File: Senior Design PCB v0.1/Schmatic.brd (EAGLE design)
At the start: 101.3 x 67.5 mm, 243 parts, among them IC1 TMC2208, IC2 TMC2208, IC3 TMC2208, IC4 TMC2208, IC5 TMC2208, IC6 CP2104, Q1 mmbt2222, Q2 mmbt2222, Q3 MMBT4403, Q4 AOD417, Q5 MMBT4403, Q6 MMBT4403, Q7 DMG3415U, U1 PCA9685, U2 AP2112-3.3, U3 HTU21DF, U4 HX711, U5 HX711, U6 HX711, U7 SX1509, X2 ESP32_WROOM32_SKINNY

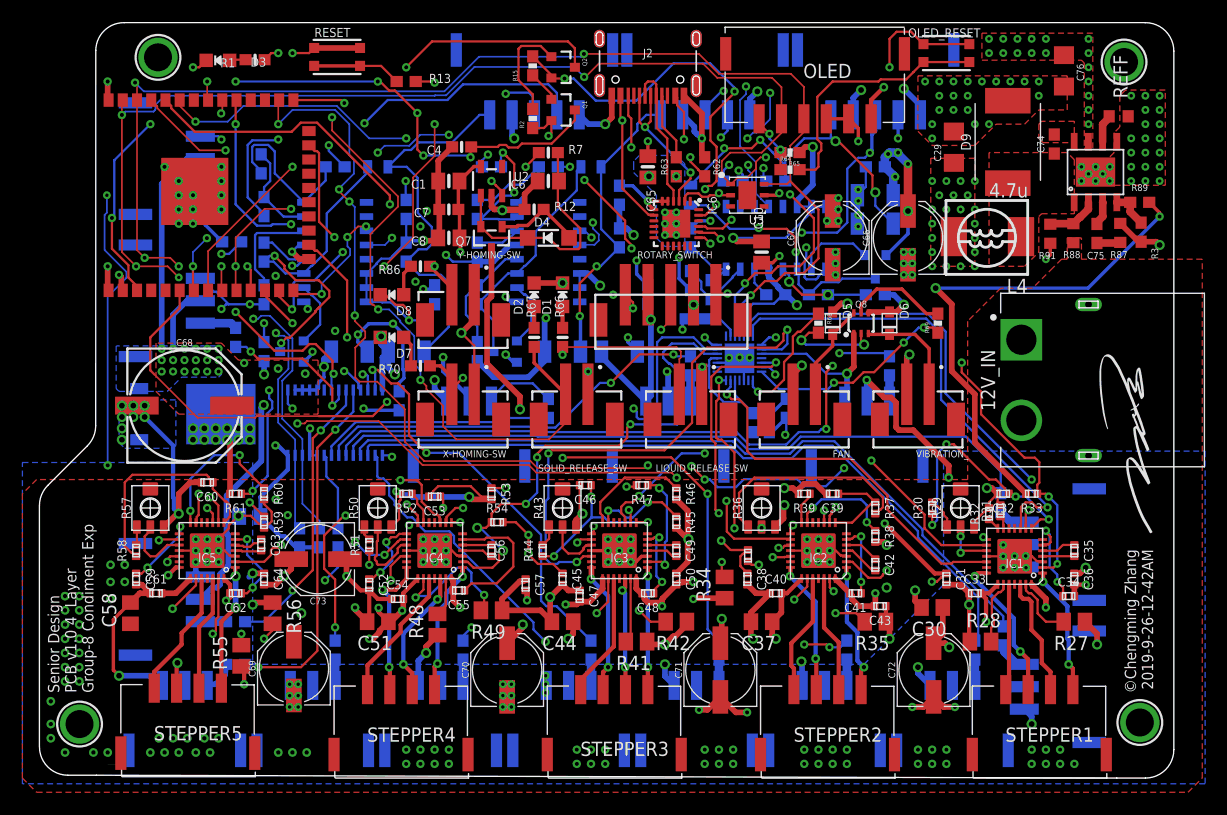
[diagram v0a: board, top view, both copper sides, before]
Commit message: added another buck converter for 5v to 3v3
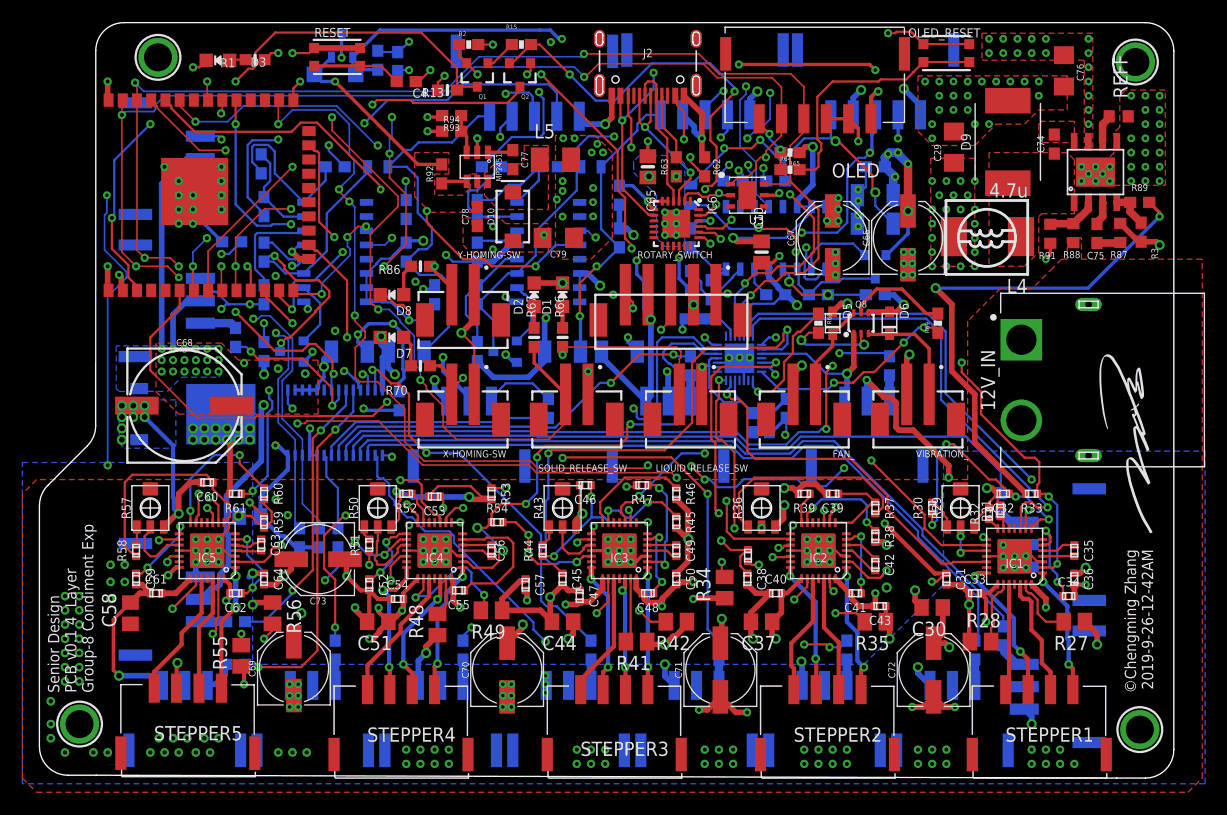
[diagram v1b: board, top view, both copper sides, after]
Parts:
- removed C1: 10uF, microbuilder:0805-NO
- removed C6, C8: 10µF, microbuilder:0805-NO
- removed C7: 1uF, microbuilder:0603-NO
- removed R7: 100K, microbuilder:0603-NO
- removed U2: AP2112-3.3, microbuilder:SOT23-5
- added C77, C78, C80: 0.1uF, SparkFun-Capacitors:0603
- added C79: 4.7uF, SparkFun-Capacitors:1206
- added D10: 3A/40V/500mV, SparkFun-DiscreteSemi:SMA-DIODE
- added L5: SWPA3012S4R7MT, rcl:L3230M
- added MP2451: MP2451, NewKevinMade:TSOT-23-6-SOT-23-6
- added R92: 100K, SparkFun-Resistors:0603
- added R93: 124K, SparkFun-Resistors:0603
- added R94: 40.2k, SparkFun-Resistors:0603
- R3: value 210k -> 40.2K
- R89: value 40.2K -> 210K
- moved D4 24.0 mm to (20.3, 61.6), flipped to the bottom, turned to 180 degrees
- moved Q7 21.7 mm to (21.0, 64.1), flipped to the bottom, turned to 0 degrees
- moved R12 19.3 mm to (24.1, 62.9), flipped to the bottom, turned to 270 degrees
- moved R2 8.73 mm to (32.3, 64.3), turned to 0 degrees
- moved Q1 8.25 mm to (33.0, 61.6), turned to 180 degrees
- moved C4 5.24 mm to (30.4, 60.2)
- moved Q2 3.86 mm to (36.8, 61.6), turned to 180 degrees
- moved R15 2.16 mm to (37.0, 64.3), turned to 180 degrees
- moved U$50 1.02 mm to (91.8, 62.7)
- moved U$48 0.63 mm to (92.2, 3.06)
- moved WEIGHT1 0.13 mm to (29.2, 67.2)
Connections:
- removed net EN: R7.1, U2.3
- removed net N$26: IC6.8, J2.VBUS1, J2.VBUS2
- removed net N$7: C6.1, D4.C, Q7.2, R7.2, U2.1
- new net 3V3_FB: MP2451.PIN3, R93.1, R94.2
- new net N$25: MP2451.PIN4, R92.1
- new net N$29: C77.1, MP2451.PIN1
- new net N$31: C77.2, D10.C, L5.1, MP2451.PIN6
- new net VIN: C78.2, D4.C, MP2451.PIN5, Q7.2, R92.2
- net GND: now also C78.1, C79.2, C80.1, D10.A, MP2451.PIN2, R94.1; no longer C1.2, C6.2, C7.2, C8.2, U2.2
- net VBUS: now also IC6.8, J2.VBUS1, J2.VBUS2
- net VCC: now also C79.1, C80.2, L5.2, R93.2; no longer C1.1, C7.1, C8.1, U2.5
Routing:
- net VBUS: track 7.83 -> 61.6 mm, vias 0 -> 4
- net 5V_REG: track 133.3 -> 183.1 mm, vias 51 -> 54
- net N$26: track 22.7 -> 0.00 mm, vias 2 -> 0
- net N$7: track 22.0 -> 0.00 mm
- net VIN: track 0.00 -> 16.9 mm, vias 0 -> 1
- net GND: track 461.9 -> 449.4 mm, vias 228 -> 234
- net RTS: track 25.2 -> 37.0 mm
- net RESET: track 64.5 -> 54.0 mm, vias 7 -> 3
- net VCC: track 146.4 -> 136.9 mm, vias 37 -> 50
- net EN: track 7.03 -> 0.00 mm, vias 2 -> 0
- net SDA: track 152.7 -> 147.0 mm
- net GPIO0: track 29.5 -> 24.0 mm
- net WEIGHT_CLK_1: track 77.2 -> 81.0 mm, vias 6 -> 7
- net 3V3_FB: track 0.00 -> 3.47 mm
- net N$16: track 13.3 -> 10.2 mm, vias 2 -> 0
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- added copper zone on layer 1, net N$31
- added copper zone on layer 1, net VCC
- added copper zone on layer 1, net VIN
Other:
- board text added: "Senior Design PCB v0.1 4 Layer Group-8 Condiment Exp"
- board text removed: "Senior Design PCB v1.0 4 Layer Group-8 Condiment Exp"
